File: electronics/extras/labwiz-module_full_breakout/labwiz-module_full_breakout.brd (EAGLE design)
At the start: 64 x 33.2 mm, 8 parts

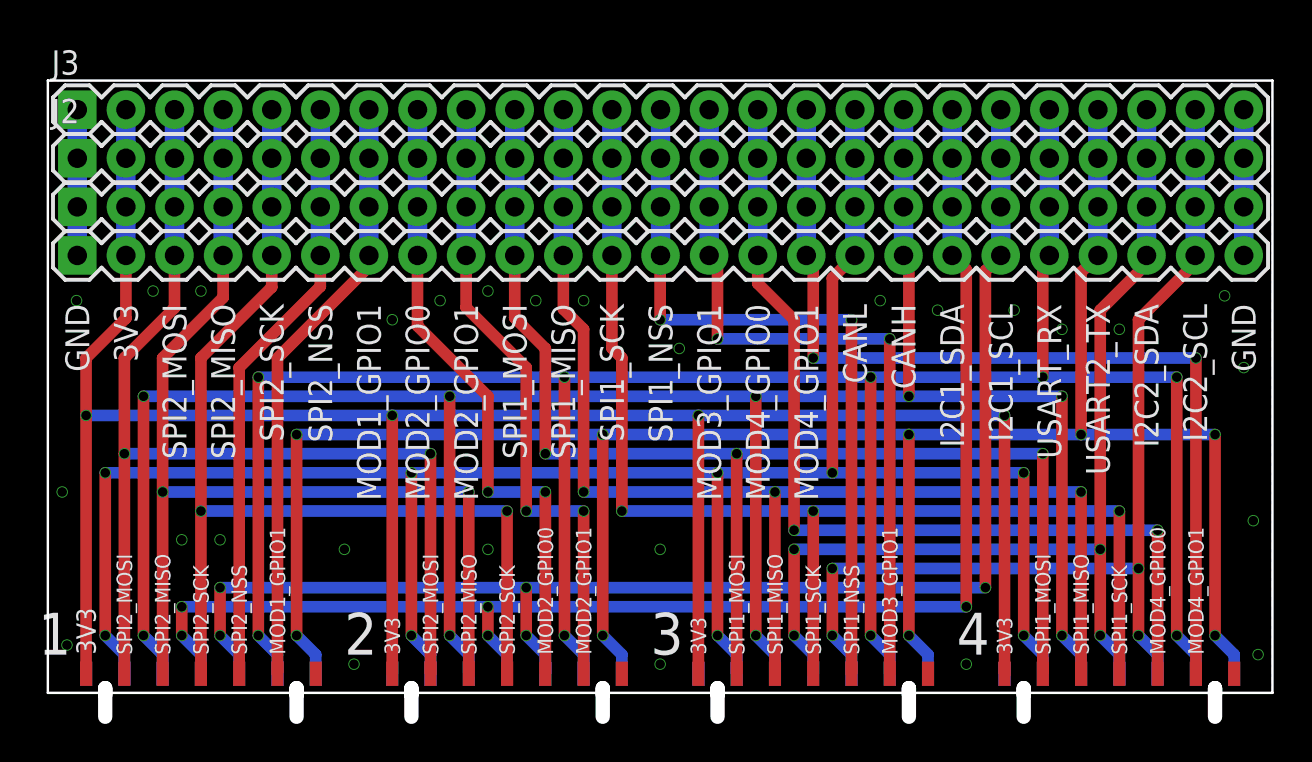
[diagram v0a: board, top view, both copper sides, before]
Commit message: Minor changes after design review. Will begin generating new gerbrs.
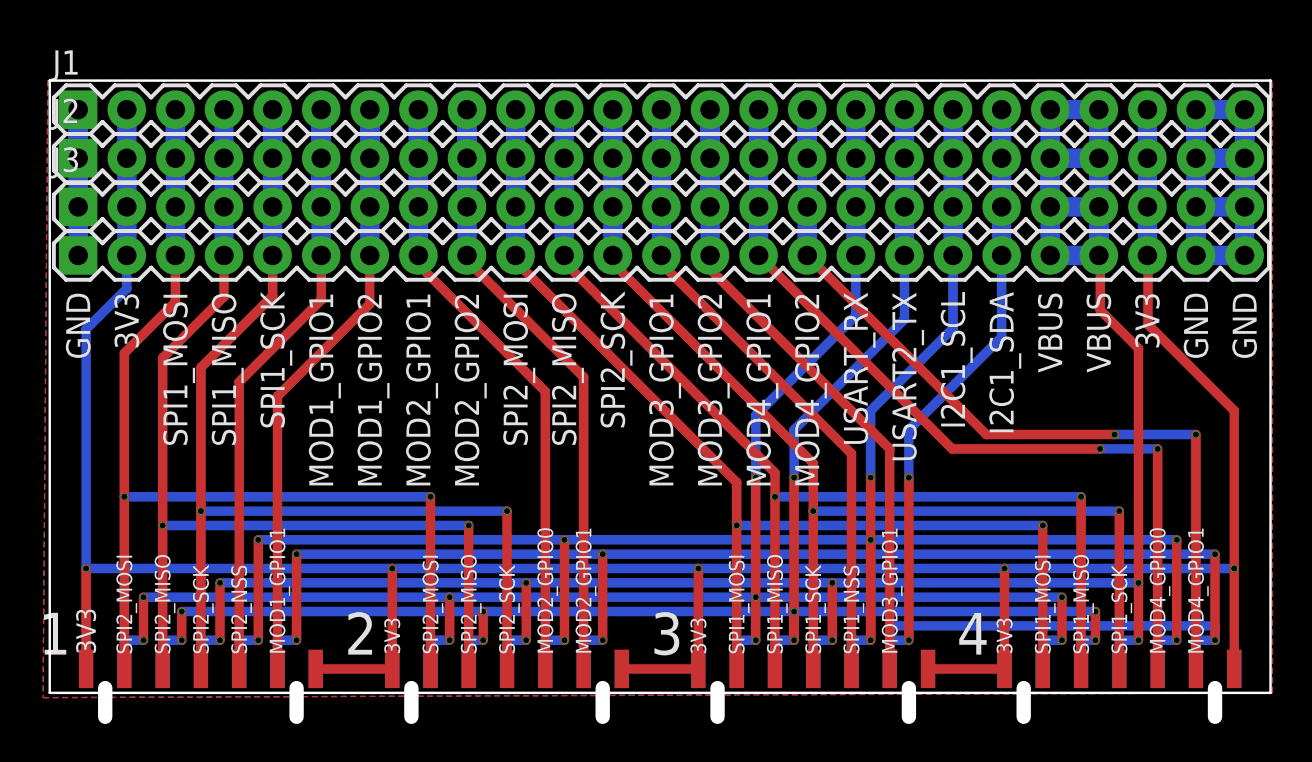
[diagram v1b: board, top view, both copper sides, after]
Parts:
- moved J1 5.08 mm to (1.59, 30.5)
- moved J3 5.08 mm to (1.59, 25.4)
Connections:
- removed net CANH: J1.18, J2.18, J3.18, J4.18, MODULE5.P$10, MODULE6.P$10, MODULE7.P$10, MODULE8.P$10
- removed net CANL: J1.17, J2.17, J3.17, J4.17, MODULE5.P$12, MODULE6.P$12, MODULE7.P$12, MODULE8.P$12
- removed net I2C2_SCL: J1.24, J2.24, J3.24, J4.24, MODULE7.P$6, MODULE8.P$6
- removed net I2C2_SDA: J1.23, J2.23, J3.23, J4.23, MODULE7.P$8, MODULE8.P$8
- removed net MOD2_GPIO0: J1.8, J2.8, J3.8, J4.8, MODULE6.P$5
- removed net MOD4_GPIO0: J1.15, J2.15, J3.15, J4.15, MODULE8.P$5
- removed net SPI1_NSS: J1.13, J2.13, J3.13, J4.13, MODULE7.P$5
- removed net SPI2_NSS: J1.6, J2.6, J3.6, J4.6, MODULE5.P$5
- new net MOD1_GPIO2: J1.7, J2.7, J3.7, J4.7, MODULE5.P$3
- new net MOD2_GPIO2: J1.9, J2.9, J3.9, J4.9, MODULE6.P$3
- new net MOD3_GPIO2: J1.14, J2.14, J3.14, J4.14, MODULE7.P$3
- new net MOD4_GPIO2: J1.16, J2.16, J3.16, J4.16, MODULE8.P$3
- new net VBUS: J1.21, J1.22, J2.21, J2.22, J3.21, J3.22, J4.21, J4.22, MODULE5.P$8, MODULE6.P$8, MODULE7.P$8, MODULE8.P$8
- net 3.3V: now also J1.23, J2.23, J3.23, J4.23, MODULE5.P$1, MODULE6.P$1, MODULE7.P$1, MODULE8.P$1
- net GND: now also J1.24, J2.24, J3.24, J4.24, MODULE5.P$2, MODULE6.P$2, MODULE7.P$2, MODULE8.P$2
- net I2C1_SCL: now also J1.19, J2.19, J3.19, J4.19, MODULE7.P$6, MODULE8.P$6; no longer J1.20, J2.20, J3.20, J4.20
- net I2C1_SDA: now also J1.20, J2.20, J3.20, J4.20, MODULE5.P$4, MODULE6.P$4, MODULE7.P$4, MODULE8.P$4; no longer J1.19, J2.19, J3.19, J4.19, MODULE5.P$8, MODULE6.P$8
- net MOD1_GPIO1: now also J1.6, J2.6, J3.6, J4.6, MODULE5.P$5; no longer J1.7, J2.7, J3.7, J4.7, MODULE5.P$3
- net MOD2_GPIO1: now also J1.8, J2.8, J3.8, J4.8, MODULE6.P$5; no longer J1.9, J2.9, J3.9, J4.9, MODULE6.P$3
- net MOD3_GPIO1: now also J1.13, J2.13, J3.13, J4.13, MODULE7.P$5; no longer J1.14, J2.14, J3.14, J4.14, MODULE7.P$3
- net MOD4_GPIO1: now also J1.15, J2.15, J3.15, J4.15, MODULE8.P$5; no longer J1.16, J2.16, J3.16, J4.16, MODULE8.P$3
- net SPI1_MISO: now also J1.4, J2.4, J3.4, J4.4, MODULE5.P$9, MODULE6.P$9; no longer J1.11, J2.11, J3.11, J4.11, MODULE7.P$9, MODULE8.P$9
- net SPI1_MOSI: now also J1.3, J2.3, J3.3, J4.3, MODULE5.P$11, MODULE6.P$11; no longer J1.10, J2.10, J3.10, J4.10, MODULE7.P$11, MODULE8.P$11
- net SPI1_SCK: now also J1.5, J2.5, J3.5, J4.5, MODULE5.P$7, MODULE6.P$7; no longer J1.12, J2.12, J3.12, J4.12, MODULE7.P$7, MODULE8.P$7
- net SPI2_MISO: now also J1.11, J2.11, J3.11, J4.11, MODULE7.P$9, MODULE8.P$9; no longer J1.4, J2.4, J3.4, J4.4, MODULE5.P$9, MODULE6.P$9
- net SPI2_MOSI: now also J1.10, J2.10, J3.10, J4.10, MODULE7.P$11, MODULE8.P$11; no longer J1.3, J2.3, J3.3, J4.3, MODULE5.P$11, MODULE6.P$11
- net SPI2_SCK: now also J1.12, J2.12, J3.12, J4.12, MODULE7.P$7, MODULE8.P$7; no longer J1.5, J2.5, J3.5, J4.5, MODULE5.P$7, MODULE6.P$7
- net USART2_RX: now also J1.17, J2.17, J3.17, J4.17, MODULE5.P$12, MODULE6.P$12, MODULE7.P$12, MODULE8.P$12; no longer J1.21, J2.21, J3.21, J4.21, MODULE5.P$4, MODULE6.P$4, MODULE7.P$4, MODULE8.P$4
- net USART2_TX: now also J1.18, J2.18, J3.18, J4.18, MODULE5.P$10, MODULE6.P$10, MODULE7.P$10, MODULE8.P$10; no longer J1.22, J2.22, J3.22, J4.22, MODULE5.P$2, MODULE6.P$2, MODULE7.P$2, MODULE8.P$2
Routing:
- net CANH: track 122.8 -> 0.00 mm, vias 9 -> 0
- net VBUS: track 0.00 -> 118.4 mm, vias 0 -> 8
- net CANL: track 111.1 -> 0.00 mm, vias 9 -> 0
- net I2C2_SDA: track 53.9 -> 0.00 mm, vias 4 -> 0
- net I2C2_SCL: track 53.1 -> 0.00 mm, vias 4 -> 0
- net MOD4_GPIO0: track 49.3 -> 0.00 mm, vias 2 -> 0
- net MOD4_GPIO2: track 0.00 -> 46.6 mm, vias 0 -> 2
- net I2C1_SDA: track 75.1 -> 119.7 mm, vias 5 -> 8
- net SPI1_NSS: track 39.5 -> 0.00 mm, vias 2 -> 0
- net MOD3_GPIO2: track 0.00 -> 38.2 mm
- net MOD2_GPIO2: track 0.00 -> 36.8 mm
- net MOD1_GPIO2: track 0.00 -> 36.3 mm
- net GND: track 15.2 -> 50.8 mm, vias 28 -> 0
- net MOD2_GPIO0: track 34.0 -> 0.00 mm, vias 2 -> 0
- net I2C1_SCL: track 75.1 -> 108.5 mm, vias 5 -> 9
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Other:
- board size 64 x 33.2 mm -> 63.8 x 33.2 mm
- board text added: "MOD1_GPIO2"
- board text added: "MOD2_GPIO2"
- board text added: "MOD3_GPIO2"
- board text added: "MOD4_GPIO2"
- board text added: "VBUS"
